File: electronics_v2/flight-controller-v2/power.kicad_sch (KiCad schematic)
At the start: 14 parts

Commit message: FC scheme complete
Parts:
- J1: renamed from J?; footprint (none) -> Connector_IDC:IDC-Header_2x05_P2.54mm_Vertical
- gave numbers to parts that had none: 13
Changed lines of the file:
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@@
   (symbol (lib_id "Device:C") (at 233.68 124.46 0) (unit 1)
     (in_bom yes) (on_board yes)
-    (property "Reference" "C?" (id 0) (at 237.49 123.19 0)
+    (property "Reference" "C6" (id 0) (at 237.49 123.19 0)
       (effects (font (size 1.27 1.27)) (justify left))
     )
@@
   (symbol (lib_id "Device:C") (at 123.19 121.92 0) (unit 1)
     (in_bom yes) (on_board yes)
-    (property "Reference" "C?" (id 0) (at 125.73 120.65 0)
+    (property "Reference" "C5" (id 0) (at 125.73 120.65 0)
       (effects (font (size 1.27 1.27)) (justify left))
     )
@@
   (symbol (lib_id "Diode:BAT54S") (at 210.82 83.82 270) (mirror x) (unit 1)
     (in_bom yes) (on_board yes)
-    (property "Reference" "D?" (id 0) (at 213.36 76.2 90)
+    (property "Reference" "D1" (id 0) (at 213.36 76.2 90)
       (effects (font (size 1.27 1.27)) (justify left))
     )
@@
   (symbol (lib_id "power:+5V") (at 80.01 115.57 0) (unit 1)
     (in_bom yes) (on_board yes)
-    (property "Reference" "#PWR?" (id 0) (at 80.01 119.38 0)
+    (property "Reference" "#PWR08" (id 0) (at 80.01 119.38 0)
       (effects (font (size 1.27 1.27)) hide)
     )
@@
   (symbol (lib_id "Device:R") (at 228.6 85.09 90) (unit 1)
     (in_bom yes) (on_board yes)
-    (property "Reference" "R?" (id 0) (at 228.6 80.01 90))
+    (property "Reference" "R2" (id 0) (at 228.6 80.01 90))
     (property "Value" "16k" (id 1) (at 228.6 82.55 90))
     (property "Footprint" "Resistor_SMD:R_0603_1608Metric" (id 2) (at 228.6 86.868 90)
@@
   (symbol (lib_id "power:+3.3V") (at 210.82 76.2 0) (unit 1)
     (in_bom yes) (on_board yes) (fields_autoplaced)
-    (property "Reference" "#PWR?" (id 0) (at 210.82 80.01 0)
+    (property "Reference" "#PWR03" (id 0) (at 210.82 80.01 0)
       (effects (font (size 1.27 1.27)) hide)
     )
@@
   (symbol (lib_id "Diode:BAT54S") (at 210.82 118.11 270) (mirror x) (unit 1)
     (in_bom yes) (on_board yes)
-    (property "Reference" "D?" (id 0) (at 213.36 110.49 90)
+    (property "Reference" "D2" (id 0) (at 213.36 110.49 90)
       (effects (font (size 1.27 1.27)) (justify left))
     )
@@
   (symbol (lib_id "Connector_Generic:Conn_02x05_Odd_Even") (at 100.33 80.01 0) (unit 1)
     (in_bom yes) (on_board yes)
-    (property "Reference" "J?" (id 0) (at 101.6 68.58 0))
+    (property "Reference" "J1" (id 0) (at 101.6 68.58 0))
     (property "Value" "Conn_02x05_Odd_Even" (id 1) (at 96.52 71.12 0))
-    (property "Footprint" "" (id 2) (at 100.33 80.01 0)
+    (property "Footprint" "Connector_IDC:IDC-Header_2x05_P2.54mm_Vertical" (id 2) (at 100.33 80.01 0)
       (effects (font (size 1.27 1.27)) hide)
     )
@@
   (symbol (lib_id "Device:R") (at 199.39 83.82 90) (unit 1)
     (in_bom yes) (on_board yes)
-    (property "Reference" "R?" (id 0) (at 199.39 78.74 90))
+    (property "Reference" "R1" (id 0) (at 199.39 78.74 90))
     (property "Value" "1k" (id 1) (at 199.39 81.28 90))
     (property "Footprint" "Resistor_SMD:R_0603_1608Metric" (id 2) (at 199.39 85.598 90)
@@
   (symbol (lib_id "Device:C_Polarized") (at 91.44 121.92 0) (unit 1)
     (in_bom yes) (on_board yes)
-    (property "Reference" "C?" (id 0) (at 93.98 119.38 0)
+    (property "Reference" "C3" (id 0) (at 93.98 119.38 0)
       (effects (font (size 1.27 1.27)) (justify left))
     )
@@
   (symbol (lib_id "power:GND") (at 210.82 125.73 0) (unit 1)
     (in_bom yes) (on_board yes)
-    (property "Reference" "#PWR?" (id 0) (at 210.82 132.08 0)
+    (property "Reference" "#PWR010" (id 0) (at 210.82 132.08 0)
       (effects (font (size 1.27 1.27)) hide)
     )
@@
   (symbol (lib_id "power:GND") (at 92.71 87.63 0) (unit 1)
     (in_bom yes) (on_board yes) (fields_autoplaced)
-    (property "Reference" "#PWR?" (id 0) (at 92.71 93.98 0)
+    (property "Reference" "#PWR04" (id 0) (at 92.71 93.98 0)
       (effects (font (size 1.27 1.27)) hide)
     )
@@
   (symbol (lib_id "Device:C") (at 233.68 90.17 0) (unit 1)
     (in_bom yes) (on_board yes)
-    (property "Reference" "C?" (id 0) (at 237.49 88.9 0)
+    (property "Reference" "C1" (id 0) (at 237.49 88.9 0)
       (effects (font (size 1.27 1.27)) (justify left))
     )
@@
   (symbol (lib_id "Device:C") (at 80.01 121.92 0) (unit 1)
     (in_bom yes) (on_board yes)
-    (property "Reference" "C?" (id 0) (at 82.55 120.65 0)
+    (property "Reference" "C2" (id 0) (at 82.55 120.65 0)
       (effects (font (size 1.27 1.27)) (justify left))
     )
@@
   (symbol (lib_id "power:+3.3V") (at 123.19 115.57 0) (unit 1)
     (in_bom yes) (on_board yes) (fields_autoplaced)
-    (property "Reference" "#PWR?" (id 0) (at 123.19 119.38 0)
+    (property "Reference" "#PWR09" (id 0) (at 123.19 119.38 0)
       (effects (font (size 1.27 1.27)) hide)
     )
@@
   (symbol (lib_id "power:GND") (at 233.68 93.98 0) (unit 1)
     (in_bom yes) (on_board yes)
-    (property "Reference" "#PWR?" (id 0) (at 233.68 100.33 0)
+    (property "Reference" "#PWR06" (id 0) (at 233.68 100.33 0)
       (effects (font (size 1.27 1.27)) hide)
     )
@@
   (symbol (lib_id "power:+3.3V") (at 210.82 110.49 0) (unit 1)
     (in_bom yes) (on_board yes) (fields_autoplaced)
-    (property "Reference" "#PWR?" (id 0) (at 210.82 114.3 0)
+    (property "Reference" "#PWR07" (id 0) (at 210.82 114.3 0)
       (effects (font (size 1.27 1.27)) hide)
     )
@@
   (symbol (lib_id "power:GND") (at 233.68 128.27 0) (unit 1)
     (in_bom yes) (on_board yes)
-    (property "Reference" "#PWR?" (id 0) (at 233.68 134.62 0)
+    (property "Reference" "#PWR012" (id 0) (at 233.68 134.62 0)
       (effects (font (size 1.27 1.27)) hide)
     )
@@
   (symbol (lib_id "Device:R") (at 199.39 118.11 90) (unit 1)
     (in_bom yes) (on_board yes)
-    (property "Reference" "R?" (id 0) (at 199.39 113.03 90))
+    (property "Reference" "R3" (id 0) (at 199.39 113.03 90))
     (property "Value" "1k" (id 1) (at 199.39 115.57 90))
     (property "Footprint" "Resistor_SMD:R_0603_1608Metric" (id 2) (at 199.39 119.888 90)
@@
   (symbol (lib_id "Regulator_Linear:LM1117-3.3") (at 102.87 116.84 0) (unit 1)
     (in_bom yes) (on_board yes) (fields_autoplaced)
-    (property "Reference" "U?" (id 0) (at 102.87 109.22 0))
+    (property "Reference" "U1" (id 0) (at 102.87 109.22 0))
     (property "Value" "LM1117-3.3" (id 1) (at 102.87 111.76 0))
     (property "Footprint" "Package_TO_SOT_SMD:SOT-223-3_TabPin2" (id 2) (at 102.87 116.84 0)
@@
   (symbol (lib_id "power:GND") (at 210.82 91.44 0) (unit 1)
     (in_bom yes) (on_board yes) (fields_autoplaced)
-    (property "Reference" "#PWR?" (id 0) (at 210.82 97.79 0)
+    (property "Reference" "#PWR05" (id 0) (at 210.82 97.79 0)
       (effects (font (size 1.27 1.27)) hide)
     )
@@
   (symbol (lib_id "power:+5V") (at 110.49 72.39 0) (unit 1)
     (in_bom yes) (on_board yes)
-    (property "Reference" "#PWR?" (id 0) (at 110.49 76.2 0)
+    (property "Reference" "#PWR02" (id 0) (at 110.49 76.2 0)
       (effects (font (size 1.27 1.27)) hide)
     )
@@
   (symbol (lib_id "power:GND") (at 102.87 128.27 0) (unit 1)
     (in_bom yes) (on_board yes) (fields_autoplaced)
-    (property "Reference" "#PWR?" (id 0) (at 102.87 134.62 0)
+    (property "Reference" "#PWR011" (id 0) (at 102.87 134.62 0)
       (effects (font (size 1.27 1.27)) hide)
     )
@@
   (symbol (lib_id "Device:C_Polarized") (at 113.03 121.92 0) (unit 1)
     (in_bom yes) (on_board yes)
-    (property "Reference" "C?" (id 0) (at 115.57 119.38 0)
+    (property "Reference" "C4" (id 0) (at 115.57 119.38 0)
       (effects (font (size 1.27 1.27)) (justify left))
     )
@@
   (symbol (lib_id "Device:R") (at 228.6 119.38 90) (unit 1)
     (in_bom yes) (on_board yes)
-    (property "Reference" "R?" (id 0) (at 228.6 114.3 90))
+    (property "Reference" "R4" (id 0) (at 228.6 114.3 90))
     (property "Value" "16k" (id 1) (at 228.6 116.84 90))
     (property "Footprint" "Resistor_SMD:R_0603_1608Metric" (id 2) (at 228.6 121.158 90)

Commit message: edge XT60 connector & INA226 I2C measurement
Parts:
- removed C1, C6: 100n, Capacitor_SMD:C_0603_1608Metric, symbol Device:C
- removed D1, D2: BAT54S, Package_TO_SOT_SMD:SOT-23, symbol Diode:BAT54S
- removed R1, R3: 1k, Resistor_SMD:R_0603_1608Metric, symbol Device:R
- removed R2, R4: 16k, Resistor_SMD:R_0603_1608Metric, symbol Device:R
- renumbered C2 to C1, C3 to C2, C4 to C3, C5 to C4
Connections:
- net BATT_I_SENSE renamed EXT_I2C_SDA
- net BATT_V_SENSE renamed EXT_I2C_SCL
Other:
- note removed: "analog measuring channels"
- note removed: "cutoff: 100 Hz"

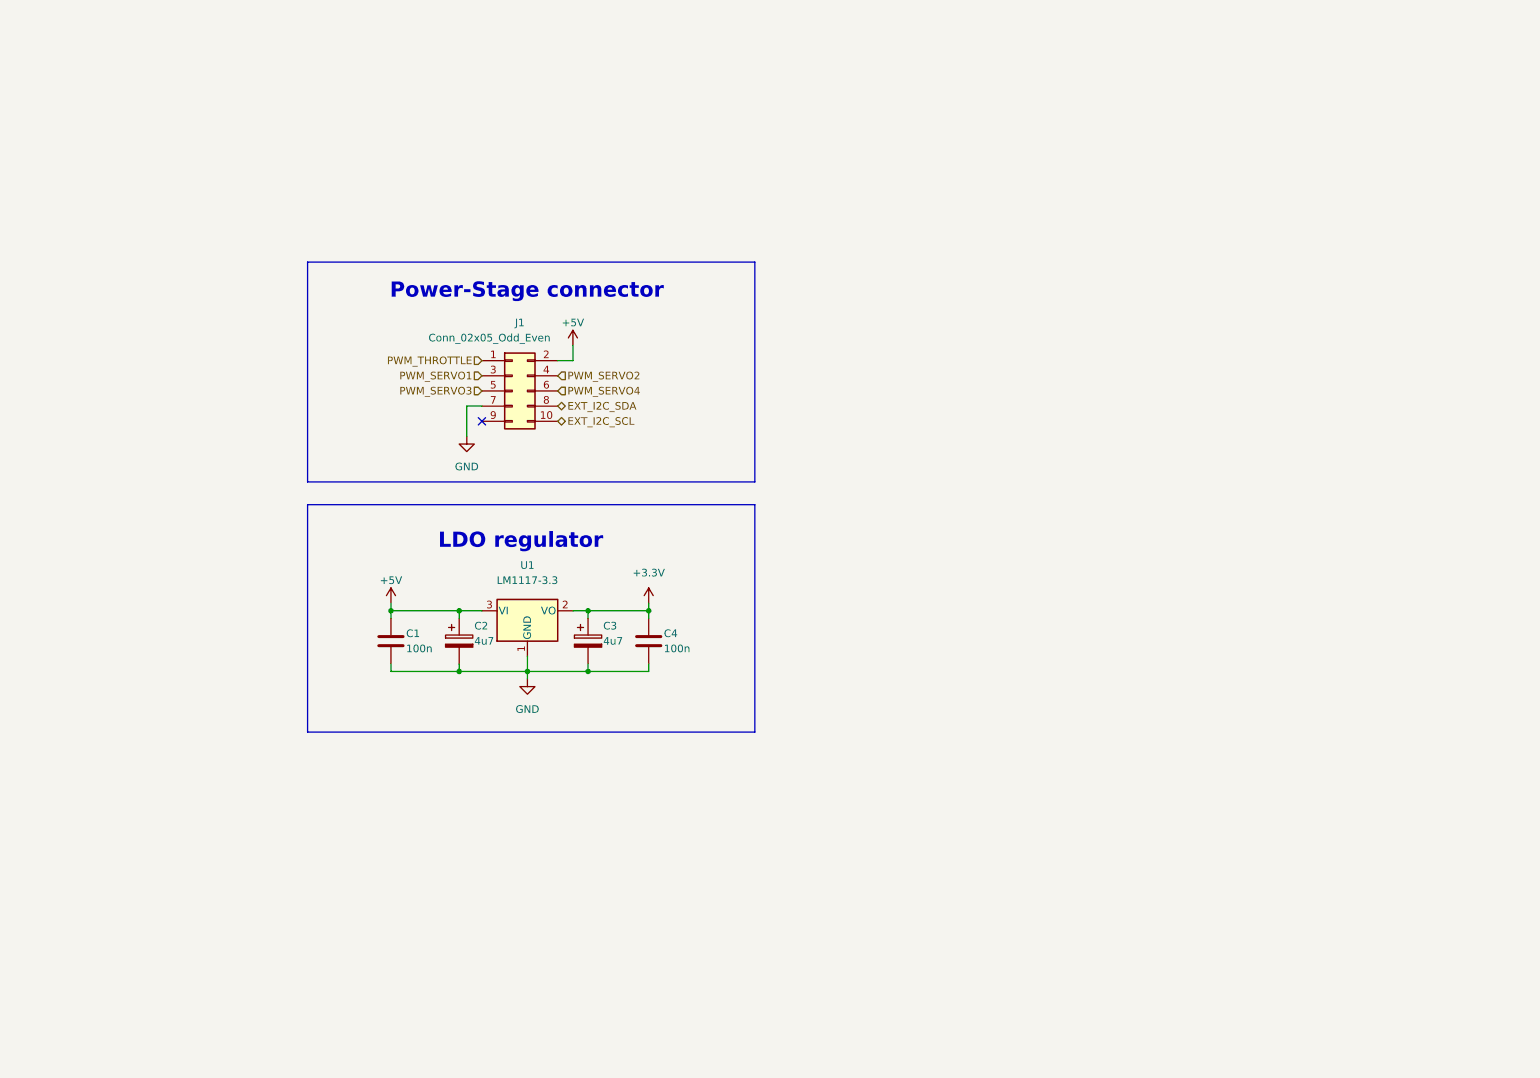
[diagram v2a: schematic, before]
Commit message: move PLI to FC
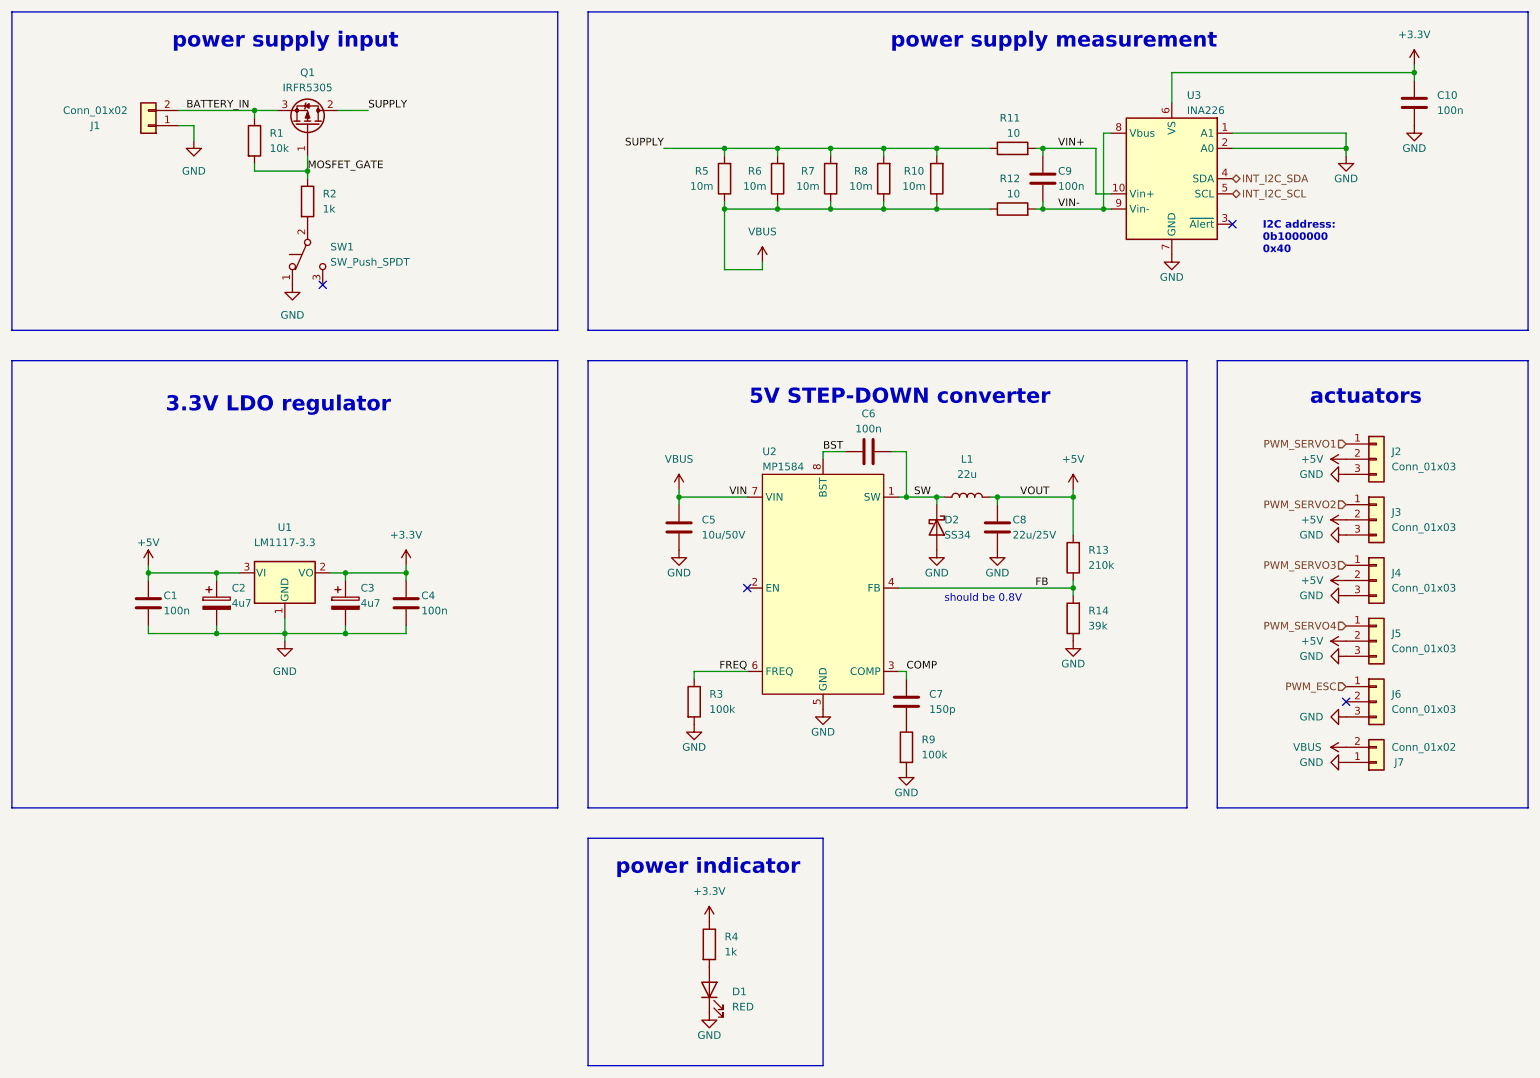
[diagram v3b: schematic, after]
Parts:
- removed J1: Conn_02x05_Odd_Even, Connector_IDC:IDC-Header_2x05_P2.54mm_Vertical, symbol Connector_Generic:Conn_02x05_Odd_Even
- added C10, C6, C9: 100n, Capacitor_SMD:C_0603_1608Metric, symbol Device:C
- added C5: 10u/50V, Capacitor_SMD:C_1206_3216Metric, symbol Device:C
- added C7: 150p, Capacitor_SMD:C_0603_1608Metric, symbol Device:C
- added C8: 22u/25V, Capacitor_SMD:C_1206_3216Metric, symbol Device:C
- added D1: RED, LED_SMD:LED_0603_1608Metric, symbol Device:LED
- added D2: SS34, Diode_SMD:D_SMA, symbol Device:D_Schottky
- added J1: Conn_01x02, Connector_AMASS:AMASS_XT60-M_1x02_P7.20mm_Vertical, symbol Connector_Generic:Conn_01x02
- added J2, J3, J4, J5, J6: Conn_01x03, Connector_PinHeader_2.54mm:PinHeader_1x03_P2.54mm_Vertical, symbol Connector_Generic:Conn_01x03
- added J7: Conn_01x02, Connector_AMASS:AMASS_XT60-F_1x02_P7.20mm_Vertical, symbol Connector_Generic:Conn_01x02
- added L1: 22u, Inductor_SMD:L_AVX_LMLP07A7, symbol Device:L
- added Q1: IRFR5305, Package_TO_SOT_SMD:TO-252-2, symbol Device:Q_PMOS_GDS
- added R1: 10k, Resistor_SMD:R_0603_1608Metric, symbol Device:R
- added R10, R5, R6, R7, R8: 10m, Resistor_SMD:R_1206_3216Metric, symbol Device:R
- added R11, R12: 10, Resistor_SMD:R_0603_1608Metric, symbol Device:R
- added R13: 210k, Resistor_SMD:R_0603_1608Metric, symbol Device:R
- added R14: 39k, Resistor_SMD:R_0603_1608Metric, symbol Device:R
- added R2, R4: 1k, Resistor_SMD:R_0603_1608Metric, symbol Device:R
- added R3, R9: 100k, Resistor_SMD:R_0603_1608Metric, symbol Device:R
- added SW1: SW_Push_SPDT, Button_Switch_THT:SW_CuK_JS202011CQN_DPDT_Straight, symbol Switch:SW_Push_SPDT
- added U2: MP1584, Package_SO:SOIC-8-1EP_3.9x4.9mm_P1.27mm_EP2.62x3.51mm_ThermalVias, symbol goose:MP1584
- added U3: INA226, Package_SO:VSSOP-10_3x3mm_P0.5mm, symbol Analog_ADC:INA226
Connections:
- net +5V: now also C8.2, J2.2 (Pin_2), J3.2 (Pin_2), J4.2 (Pin_2), J5.2 (Pin_2), L1.2, R13.2
- net GND: now also C10.1, C5.1, C8.1, D1.1 (K), D2.2 (A), J1.1 (Pin_1), J2.3 (Pin_3), J3.3 (Pin_3), J4.3 (Pin_3), J5.3 (Pin_3), J6.3 (Pin_3), J7.1 (Pin_1), R14.1, R3.2, R9.2, SW1.1 (A), U2.5 (GND), U3.1 (A1), U3.2 (A0), U3.7 (GND)
- net PWM_SERVO1: now also J2.1 (Pin_1)
- net PWM_SERVO2: now also J3.1 (Pin_1)
- net PWM_SERVO3: now also J4.1 (Pin_1)
- net PWM_SERVO4: now also J5.1 (Pin_1)
- new net: D1.2 (A), R4.2
- new net: C7.2, R9.1
- new net: R2.2, SW1.2 (B)
- new net +3V3: C10.2, R4.1, U3.6 (VS)
- new net BATTERY_IN: J1.2 (Pin_2), Q1.3 (S), R1.1
- new net BST: C6.1, U2.8 (BST)
- new net COMP: C7.1, U2.3 (COMP)
- new net FB: R13.1, R14.2, U2.4 (FB)
- new net FREQ: R3.1, U2.6 (FREQ)
- new net INT_I2C_SCL: U3.5 (SCL)
- new net INT_I2C_SDA: U3.4 (SDA)
- new net MOSFET_GATE: Q1.1 (G), R1.2, R2.1
- new net PWM_ESC: J6.1 (Pin_1)
- new net SUPPLY: Q1.2 (D), R10.2, R11.1, R5.2, R6.2, R7.2, R8.2
- new net SW: C6.2, D2.1 (K), L1.1, U2.1 (SW)
- new net VBUS: C5.2, J7.2 (Pin_2), R10.1, R12.1, R5.1, R6.1, R7.1, R8.1, U2.7 (VIN)
- new net VIN+: C9.2, R11.2, U3.10 (Vin+)
- new net VIN-: C9.1, R12.2, U3.8 (Vbus), U3.9 (Vin-)
- no-connect marks 1 -> 4
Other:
- note added: "3.3V LDO regulator"
- note added: "5V STEP-DOWN converter"
- note added: "I2C address: 0b1000000 0x40"
- note added: "actuators"
- note added: "power indicator"
- note added: "power supply input"
- note added: "power supply measurement"
- note added: "should be 0.8V"
- note removed: "LDO regulator"
- note removed: "Power-Stage connector"
- moved on the sheet: C1, C2, C3, C4, U1
